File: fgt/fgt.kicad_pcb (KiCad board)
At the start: 2 copper layers, 78 x 78 mm, 51 parts, among them J1 Conn_01x03, J2 USB_B_Mini, J3 BL_Conn, J4 Conn_01x06, Q1 BC817, SW1 Reset, SW2 SW-, SW3 SW_M/BOOT, SW4 SW+, U1 ESP32-C3-WROOM-02, U2 ERC12864, U3 BMP280, U4 HT75xx-1-SOT89

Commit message: placing locating holes
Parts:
- added H1: MountingHole, MountingHole:MountingHole_3.2mm_M3_DIN965, F.Cu at (150.0, 84.0)
- added H2: MountingHole, MountingHole:MountingHole_3.2mm_M3_DIN965, F.Cu at (90.0, 84.0)
- added H3: MountingHole, MountingHole:MountingHole_3.2mm_M3_DIN965, F.Cu at (150.0, 135.0)
- added H4: MountingHole, MountingHole:MountingHole_3.2mm_M3_DIN965, F.Cu at (90.0, 135.0)
- added J5: Conn_01x02, Connector_Phoenix_MSTB:PhoenixContact_MSTBVA_2,5_2-G-5,08_1x02_P5.08mm_Vertical, F.Cu at (117.2, 127.0)
- J1: value Conn_01x03 -> Conn_01x02; footprint Connector_Phoenix_MC:PhoenixContact_MCV_1,5_3-G-3.5_1x03_P3.50mm_Vertical -> Connector_Phoenix_MSTB:PhoenixContact_MSTBVA_2,5_2-G-5,08_1x02_P5.08mm_Vertical
- moved C22 7.28 mm to (92.5, 130.0), turned to 90 degrees
- moved SW1 4.47 mm to (87.0, 130.0), turned to 0 degrees
- moved J1 1.24 mm to (99.0, 107.5)
- moved C23 1.00 mm to (139.5, 141.0)
- moved C25 1.00 mm to (100.5, 140.8)
- moved SW2 1.00 mm to (145.0, 141.0)
- moved SW4 1.00 mm to (95.0, 141.0)
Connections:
- J1 pad 2: Earth -> /AC_L
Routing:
- net /AC_N: track 0.00 -> 33.1 mm
- net /AC_L: track 0.00 -> 16.3 mm
- net /CHIP_PU: track 123.7 -> 115.7 mm
- net GND: track 69.2 -> 76.9 mm, vias 60 -> 67
- net +5V: track 0.00 -> 4.38 mm, vias 13 -> 14
- net USB_D-: track 3.60 -> 7.14 mm
- net USB_D+: track 4.26 -> 7.78 mm
- net /SW+: track 97.1 -> 96.1 mm
- net /SW-: track 73.6 -> 72.6 mm
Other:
- outline, holes or cut-outs redrawn

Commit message: layout done v1.0.0
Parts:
- removed J5: Conn_01x02, Connector_Phoenix_MSTB:PhoenixContact_MSTBVA_2,5_2-G-5,08_1x02_P5.08mm_Vertical
- added H5: MountingHole, MountingHole:MountingHole_3.2mm_M3_DIN965, F.Cu at (133.8, 81.5)
- added H6: MountingHole, MountingHole:MountingHole_3.2mm_M3_DIN965, F.Cu at (106.3, 81.5)
- added REF**: KiCad-Logo2_5mm_SilkScreen, Symbol:KiCad-Logo2_5mm_SilkScreen, F.Cu at (98.8, 96.8)
- added REF**: OSHW-Logo2_7.3x6mm_SilkScreen, Symbol:OSHW-Logo2_7.3x6mm_SilkScreen, F.Cu at (104.8, 74.5)
- added REF**: WEEE-Logo_4.2x6mm_SilkScreen, Symbol:WEEE-Logo_4.2x6mm_SilkScreen, F.Cu at (110.5, 74.8)
- renumbered REF** to Display
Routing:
- net +3V3: track 170.9 -> 207.9 mm, vias 0 -> 1
- net /BOOT: track 73.7 -> 107.4 mm, vias 1 -> 2
- net /TXD: track 0.00 -> 29.5 mm, vias 0 -> 2
- net /RXD: track 0.00 -> 28.2 mm, vias 0 -> 2
- net USB_D-: track 7.14 -> 31.8 mm, vias 0 -> 1
- net USB_D+: track 7.78 -> 32.1 mm, vias 0 -> 1
- net /VBUS: track 2.54 -> 19.6 mm, vias 1 -> 4
- net /CHIP_PU: track 115.7 -> 131.2 mm, vias 2 -> 4
- net GND: track 76.9 -> 80.5 mm, vias 67 -> 68
- net /SCL: track 48.5 -> 51.8 mm
- net /SDA: track 51.8 -> 54.6 mm

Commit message: retouch board layout v1.1.0
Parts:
- added G***: LOGO, LOGO, F.Cu at (98.4, 92.6)
- added G***: LOGO, LOGO, F.Cu at (96.8, 121.8)
- added G***: LOGO, LOGO, B.Cu at (112.6, 130.4)
- added G***: LOGO, LOGO, B.Cu at (153.6, 143.2)
- moved REF** 26.1 mm to (136.6, 75.0)
- moved REF** 23.3 mm to (89.0, 75.6)
- moved REF** 2.18 mm to (103.0, 75.8)
- moved R1 1.60 mm to (156.2, 76.5), turned to 0 degrees
- moved C1 1.25 mm to (156.2, 74.5), turned to 0 degrees
- moved J1 0.97 mm to (100.0, 107.5)
- moved Display 0.50 mm to (120.0, 102.0)
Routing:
- net GND: track 80.5 -> 79.6 mm, vias 68 -> 66
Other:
- board size 78 x 78 mm -> 77 x 77 mm
- board text added: "AC L"
- board text added: "AC N"
- board text added: "BOOT ENABLE TXD RXD 3V3"
- board text added: "By: j74a8g@gmail.com github.com/juraj8"
- board text added: "FGT"
- board text added: "Jan 2021. Rev 1.1.0"
- board text added: "TOP"

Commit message: DRC done
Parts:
- moved Q1 0.25 mm to (141.0, 99.4)
- moved C19 0.07 mm to (138.2, 99.5)
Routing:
- net GND: track 79.6 -> 83.2 mm, vias 66 -> 69
- net Net-(J3-Pad1): track 3.79 -> 4.66 mm
- net +5V: vias 14 -> 12
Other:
- outline, holes or cut-outs redrawn
- board text added: "Jan 2021. Rev ${REVISION}"
- board text removed: "Jan 2021. Rev 1.1.0"

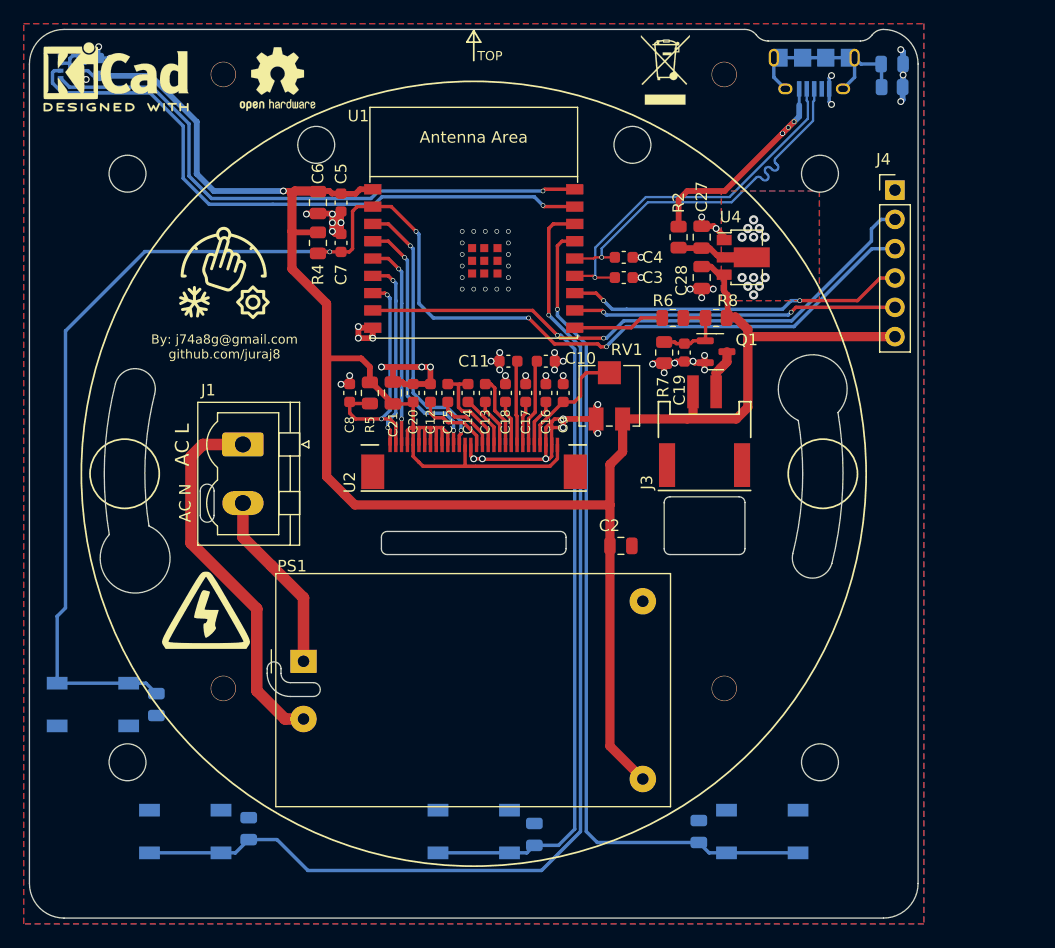
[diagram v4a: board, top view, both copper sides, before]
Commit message: Release v1.4.0 - added testpoints - fix solder mask - size down pcb
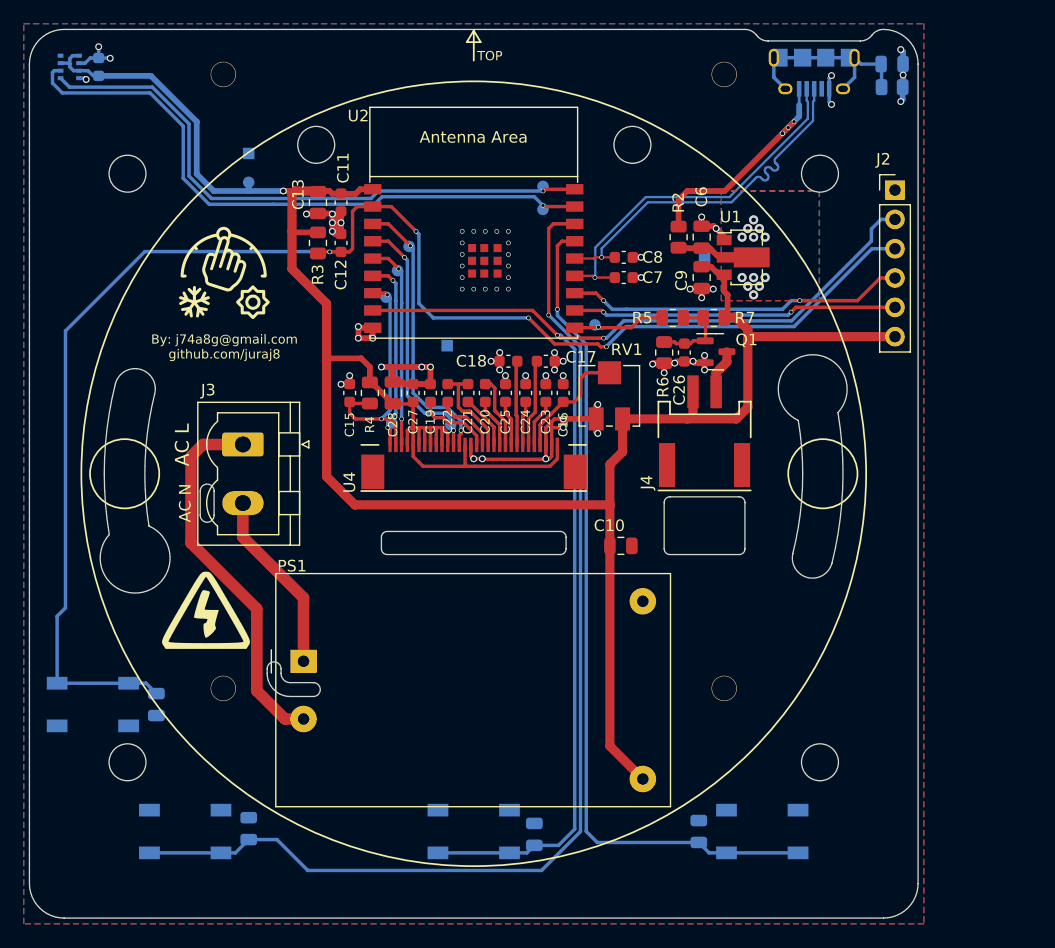
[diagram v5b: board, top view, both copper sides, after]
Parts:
- removed R8: 100K, Resistor_SMD:R_0805_2012Metric
- removed REF**: KiCad-Logo2_5mm_SilkScreen, Symbol:KiCad-Logo2_5mm_SilkScreen
- removed REF**: OSHW-Logo2_7.3x6mm_SilkScreen, Symbol:OSHW-Logo2_7.3x6mm_SilkScreen
- removed REF**: WEEE-Logo_4.2x6mm_SilkScreen, Symbol:WEEE-Logo_4.2x6mm_SilkScreen
- added R7: 100K, Resistor_SMD:R_0805_2012Metric, F.Cu at (140.8, 96.5)
- added TP1: tp, TestPoint:TestPoint_Pad_D1.0mm, B.Cu at (144.2, 91.3)
- added TP10: tp, TestPoint:TestPoint_Pad_D1.0mm, B.Cu at (130.5, 97.1)
- added TP11: tp, TestPoint:TestPoint_Pad_D1.0mm, B.Cu at (126.0, 87.1)
- added TP12: tp, TestPoint:TestPoint_Pad_D1.0mm, B.Cu at (118.0, 105.8)
- added TP13: tp, TestPoint:TestPoint_Pad_D1.0mm, B.Cu at (112.9, 105.6)
- added TP2: tp, TestPoint:TestPoint_Pad_1.0x1.0mm, B.Cu at (117.7, 98.9)
- added TP3: tp, TestPoint:TestPoint_Pad_1.0x1.0mm, B.Cu at (100.5, 82.2)
- added TP4: tp, TestPoint:TestPoint_Pad_1.0x1.0mm, B.Cu at (140.0, 91.2)
- added TP5: tp, TestPoint:TestPoint_Pad_D1.0mm, B.Cu at (100.5, 84.8)
- added TP6: tp, TestPoint:TestPoint_Pad_D1.0mm, B.Cu at (126.0, 85.1)
- added TP7: tp, TestPoint:TestPoint_Pad_D1.0mm, B.Cu at (114.4, 90.3)
- added TP8: tp, TestPoint:TestPoint_Pad_D1.0mm, B.Cu at (113.4, 92.4)
- added TP9: tp, TestPoint:TestPoint_Pad_D1.0mm, B.Cu at (112.4, 94.7)
- moved G*** 1.36 mm to (111.2, 130.2)
- renumbered C2 to C10, C5 to C11, C7 to C12, C6 to C13, C26 to C14, C8 to C15, C9 to C16, C10 to C17, C11 to C18, C12 to C19, C22 to C2, C13 to C20, C14 to C21, C15 to C22, C16 to C23, C17 to C24, C18 to C25, C19 to C26, C20 to C27, C21 to C28, C23 to C3, C24 to C4, C25 to C5, C27 to C6, C3 to C7, C4 to C8, C28 to C9, J2 to J1, J4 to J2, J1 to J3, J3 to J4, R4 to R3, R5 to R4, R6 to R5, R7 to R6, U4 to U1, U1 to U2, U2 to U4
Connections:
- C26 pad 1: Net-(C19-Pad1) (its old number) -> /display/_lcd_bck_cnt
- Q1 pad 1: Net-(C19-Pad1) (its old number) -> /display/_lcd_bck_cnt
- R5 pad 1: Net-(C19-Pad1) (its old number) -> /display/_lcd_bck_cnt
- R6 pad 1: Net-(C19-Pad1) (its old number) -> /display/_lcd_bck_cnt
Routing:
- net Net-(C19-Pad1) (its old number): track 7.63 -> 0.00 mm
- net /display/_lcd_bck_cnt: track 0.00 -> 7.63 mm
- net /LCD_BCK: track 7.94 -> 8.69 mm, vias 0 -> 1
- net +3V3: track 207.9 -> 208.7 mm
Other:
- board text added: "BOOT RESET TXD RXD 3V3"
- board text added: "G"
- board text added: "IP Address"
- board text removed: "BOOT ENABLE TXD RXD 3V3"

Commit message: Release v1.5.0 - See changelog for changes.
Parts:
- removed C8: 22pF, Capacitor_SMD:C_0603_1608Metric
- removed C9: 10uF, Capacitor_SMD:C_0805_2012Metric
- removed J1: USB_B_Mini, Connector_USB:USB_Micro-B_Amphenol_10118194_Horizontal
- removed TP10, TP11, TP12, TP9: tp, TestPoint:TestPoint_Pad_D1.0mm
- removed U1: HT75xx-1-SOT89, Package_TO_SOT_SMD:SOT-89-3
- added BT1: Battery, ER-CON30HB:ER-CON2.0-2P-SMD, F.Cu at (140.5, 123.9)
- added C31: 22uF, Capacitor_SMD:C_0805_2012Metric, F.Cu at (131.5, 124.0)
- added D1: NTS245SFT1G, Diode_SMD:D_SOD-123, F.Cu at (134.8, 125.2)
- added J5: MAIN, Connector_IDC:IDC-Header_2x03_P2.54mm_Vertical, F.Cu at (117.5, 134.8)
- added JP1: SolderJumper_2_Bridged, Jumper:SolderJumper-2_P1.3mm_Bridged_RoundedPad1.0x1.5mm, F.Cu at (166.8, 134.8)
- added L1: 10uH, Inductor_SMD:L_1008_2520Metric, F.Cu at (135.0, 130.2)
- added Q2: IRLML6302, Package_TO_SOT_SMD:SOT-23, F.Cu at (134.1, 90.7)
- added R10: R_Small, Resistor_SMD:R_0805_2012Metric, F.Cu at (128.2, 124.5)
- added R11: 75k, Resistor_SMD:R_0805_2012Metric, F.Cu at (133.1, 87.3)
- added R8: 100, Resistor_SMD:R_0805_2012Metric, F.Cu at (129.8, 133.0)
- added R9: R_Small, Resistor_SMD:R_0805_2012Metric, F.Cu at (128.2, 122.5)
- added U5: MT3608, Package_TO_SOT_SMD:SOT-23-6, F.Cu at (131.0, 128.8)
- C1, R1: moved to F.Cu
- C17, C20: value 1uF -> 0.1uF
- C19, C26: value 0.1uF -> 1uF
- C6: value 10uF -> 22uF
- C7: value 22pF -> 0.1uF; footprint Capacitor_SMD:C_0603_1608Metric -> Capacitor_SMD:C_0805_2012Metric
- R2: value 0R -> 240k
- R5: value 10K -> 100K
- R6: value 100K -> 10K
- TP2, TP3, TP4: footprint TestPoint:TestPoint_Pad_1.0x1.0mm -> TestPoint:TestPoint_Pad_D1.0mm
- moved C6 42.0 mm to (137.8, 131.5), turned to -90 degrees
- moved C7 40.0 mm to (131.8, 133.0), turned to -90 degrees
- moved R1 28.9 mm to (131.1, 90.7), turned to 90 degrees
- moved C1 28.2 mm to (131.1, 87.3), turned to 90 degrees
- moved TP4 26.7 mm to (117.9, 106.3), turned to 180 degrees
- moved R4 26.0 mm to (136.3, 97.0), turned to 180 degrees
- moved R6 25.7 mm to (111.0, 103.0)
- moved TP1 19.3 mm to (125.9, 85.3), turned to 180 degrees
- moved TP8 19.2 mm to (132.1, 96.7)
- moved TP3 16.8 mm to (115.1, 90.5)
- moved C26 15.9 mm to (122.8, 103.0)
- moved TP6 15.7 mm to (112.7, 93.5)
- moved TP5 14.8 mm to (113.3, 92.1), turned to 180 degrees
- moved TP2 14.4 mm to (125.9, 87.1)
- moved C23 8.50 mm to (117.8, 103.0), turned to 90 degrees
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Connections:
- net /AC_L renamed /Power/AC_L
- net /AC_N renamed /Power/AC_N
- C1 pad 1: Net-(C1-Pad1) -> /V_bat_adc
- C16 pad 1: Net-(C16-Pad1) -> /display/_lcd_bck_cnt
- C17 pad 1: GND -> Net-(C17-Pad1)
- C17 pad 2: Net-(C17-Pad2) -> GND
- C19 pad 1: Net-(C19-Pad1) -> GND
- C19 pad 2: GND -> Net-(C19-Pad2)
- C20 pad 2: Net-(C20-Pad2) -> GND
- C22 pad 2: Net-(C21-Pad1) -> Net-(C22-Pad2)
- C23 pad 1: GND -> Net-(C23-Pad1)
- C23 pad 2: Net-(C23-Pad2) -> Net-(C22-Pad1)
- C26 pad 1: /display/_lcd_bck_cnt -> GND
- C26 pad 2: GND -> Net-(C26-Pad2)
- C4 pad 2: /BOOT -> /SWM
- C6 pad 1: +5V -> V_BAT
- C7 pad 1: USB_D- -> V_BAT
- J2 pad 2: /BOOT -> /TXD
- J2 pad 3: /CHIP_PU -> /RXD
- J2 pad 4: /TXD -> /CHIP_PU
- J2 pad 5: /RXD -> /SWM
- R1 pad 1: Net-(C1-Pad1) -> V_BAT
- R1 pad 2: GND -> B_CHECK
- R2 pad 1: /VBUS -> Net-(Q2-Pad3)
- R2 pad 2: +5V -> /V_bat_adc
- R4 pad 1: +3V3 -> /display/_lcd_bck_cnt
- R4 pad 2: /LCD_RST -> B_CHECK
- R5 pad 2: /LCD_BCK -> GND
- R6 pad 1: /display/_lcd_bck_cnt -> +3V3
- R6 pad 2: GND -> /LCD_RST
- RV1 pad 2: Net-(C16-Pad1) -> Net-(C17-Pad1)
- SW3 pad 2: /BOOT -> /SWM
- TP1 pad 1: +5V -> /SCL
- TP2 pad 1: GND -> /SDA
- TP3 pad 1: GND -> /SPI_MOSI
- TP4 pad 1: GND -> /SPI_SCK
- TP5 pad 1: +3V3 -> /LCD_DC
- TP6 pad 1: /SCL -> /SPI_CS
- TP7 pad 1: /SPI_MOSI -> /LCD_RST
- TP8 pad 1: /LCD_DC -> B_CHECK
- U2 pad 10: /LCD_BCK -> B_CHECK
- U2 pad 13: USB_D- -> /SW-
- U2 pad 14: USB_D+ -> /SW+
- U2 pad 15: /SW- -> /DATA
- U2 pad 16: /SW+ -> /V_bat_adc
- U2 pad 8: /BOOT -> /SWM
- U4 pad 10: Net-(C20-Pad2) -> Net-(C21-Pad2)
- U4 pad 11: Net-(C20-Pad1) -> Net-(C21-Pad1)
- U4 pad 12: Net-(C21-Pad2) -> Net-(C22-Pad2)
- U4 pad 13: Net-(C21-Pad1) -> Net-(C22-Pad1)
- U4 pad 14: Net-(C22-Pad1) -> Net-(C23-Pad1)
- U4 pad 15: Net-(C19-Pad1) -> Net-(C20-Pad1)
- U4 pad 4: Net-(C16-Pad1) -> Net-(C17-Pad1)
- U4 pad 5: Net-(C23-Pad2) -> Net-(C24-Pad2)
- U4 pad 6: Net-(C17-Pad2) -> Net-(C18-Pad2)
- U4 pad 7: Net-(C24-Pad2) -> Net-(C25-Pad2)
- U4 pad 8: Net-(C18-Pad2) -> Net-(C19-Pad2)
- U4 pad 9: Net-(C25-Pad2) -> Net-(C26-Pad2)
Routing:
- net /BOOT: track 107.4 -> 0.00 mm, vias 2 -> 0
- net /SWM: track 0.00 -> 102.7 mm, vias 0 -> 1
- net V_BAT: track 0.00 -> 57.1 mm, vias 0 -> 2
- net /DATA: track 0.00 -> 54.4 mm, vias 0 -> 1
- net +3V3: track 208.7 -> 245.8 mm
- net USB_D+: track 32.1 -> 0.00 mm, vias 1 -> 0
- net USB_D-: track 31.8 -> 0.00 mm, vias 1 -> 0
- net /VBUS: track 19.6 -> 0.00 mm, vias 4 -> 0
- net GND: track 83.2 -> 65.2 mm, vias 69 -> 59
- net Net-(C1-Pad1): track 16.6 -> 0.00 mm
- net B_CHECK: track 0.00 -> 16.3 mm, vias 0 -> 3
- net Net-(C17-Pad1): track 0.00 -> 10.5 mm
- net Net-(C16-Pad1): track 10.5 -> 0.00 mm
- net /LCD_BCK: track 8.69 -> 0.00 mm, vias 1 -> 0
- net Net-(C17-Pad2): track 7.55 -> 0.00 mm
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- removed copper zone on B.Cu, net +5V
- removed copper zone on F.Cu, net +5V
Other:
- outline, holes or cut-outs redrawn
- board text added: "TXD RXD RST BOOT 3V3"
- board text removed: "BOOT RESET TXD RXD 3V3"
